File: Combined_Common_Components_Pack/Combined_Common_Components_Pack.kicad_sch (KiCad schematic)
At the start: 15 parts, among them J4 TP_hole_1.5mm, J5 TP_loop_2.54mm, J6 TP_pad_1mm, J8 Conn_01x03_Socket, K1 G5LE-1, Q12 2N7002K

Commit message: More circuits
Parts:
- added F5: 10mm Blade Fuse, Library:Fuseholder_Blade_Mini, symbol Device:Fuse
- F1: LCSC C22446878 -> C516070; Observations (none) -> 30V 200mA
- R83: Type SMD -> (none)
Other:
- note added: "Fuses"
- note added: "Optocoupler and LEDs"
- note added: "Signal, power switching, load protection"
- note removed: "Safety"
- moved on the sheet: BZ1, D26, D27, F2, H1, J4, J5, J6, J8, K1, Q12, R83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

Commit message: Added some connectors and basic parts
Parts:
- added F6: Polyfuse, Fuse:Fuse_1206_3216Metric_Pad1.42x1.75mm_HandSolder, symbol Device:Polyfuse
- added F7: Polyfuse, Fuse:Fuse_1210_3225Metric_Pad1.42x2.65mm_HandSolder, symbol Device:Polyfuse
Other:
- moved on the sheet: F2
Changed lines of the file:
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@@
+	)
+	(symbol
+		(lib_id "Device:Polyfuse")
+		(at 110.49 129.54 90)
+		(unit 1)
+		(exclude_from_sim no)
+		(in_bom yes)
+		(on_board yes)
+		(dnp no)
+		(property "Reference" "F6"
+			(at 106.426 132.334 90)
+			(effects
+				(font
+					(size 1.27 1.27)
+				)
+			)
+		)
+		(property "Value" "Polyfuse"
+			(at 112.268 132.334 90)
+			(effects
+				(font
+					(size 1.27 1.27)
+				)
+			)
+		)
+		(property "Footprint" "Fuse:Fuse_1206_3216Metric_Pad1.42x1.75mm_HandSolder"
+			(at 115.57 128.27 0)
+			(effects
+				(font
+					(size 1.27 1.27)
+				)
+				(justify left)
+				(hide yes)
+			)
+		)
+		(property "Datasheet" "~"
+			(at 110.49 129.54 0)
+			(effects
+				(font
+					(size 1.27 1.27)
+				)
+				(hide yes)
+			)
+		)
+		(property "Description" "Polymeric PTC Resettable Fuse 48V 200mA Surface Mount 1206"
+			(at 110.49 129.54 0)
+			(effects
+				(font
+					(size 1.27 1.27)
+				)
+				(hide yes)
+			)
+		)
+		(property "LCSC" "C22446878"
+			(at 110.49 129.54 0)
+			(effects
+				(font
+					(size 1.27 1.27)
+				)
+				(hide yes)
+			)
+		)
+		(property "Observations" "48V 200mA"
+			(at 110.49 127 90)
+			(effects
+				(font
+					(size 1.27 1.27)
+				)
+			)
+		)
+		(pin "1"
+		)
+		(pin "2"
+		)
+		(instances
+			(project "Combined_Common_Components_Pack"
+				(path "/59e42e8e-5444-465a-b7a8-ffbd342a8d49"
+					(reference "F6")
+					(unit 1)
+				)
+			)
+		)
 	)
 	(symbol
@@
 	)
 	(symbol
+		(lib_id "Device:Polyfuse")
+		(at 123.19 129.54 90)
+		(unit 1)
+		(exclude_from_sim no)
+		(in_bom yes)
+		(on_board yes)
+		(dnp no)
+		(property "Reference" "F7"
+			(at 119.126 132.334 90)
+			(effects
+				(font
+					(size 1.27 1.27)
+				)
+			)
+		)
+		(property "Value" "Polyfuse"
+			(at 124.968 132.334 90)
+			(effects
+				(font
+					(size 1.27 1.27)
+				)
+			)
+		)
+		(property "Footprint" "Fuse:Fuse_1210_3225Metric_Pad1.42x2.65mm_HandSolder"
+			(at 128.27 128.27 0)
+			(effects
+				(font
+					(size 1.27 1.27)
+				)
+				(justify left)
+				(hide yes)
+			)
+		)
+		(property "Datasheet" "https://www.lcsc.com/datasheet/C269167.pdf"
+			(at 123.19 129.54 0)
+			(effects
+				(font
+					(size 1.27 1.27)
+				)
+				(hide yes)
+			)
+		)
+		(property "Description" "Polymeric PTC Resettable Fuse 16V 1.5A Surface Mount 1210"
+			(at 123.19 129.54 0)
+			(effects
+				(font
+					(size 1.27 1.27)
+				)
+				(hide yes)
+			)
+		)
+		(property "LCSC" "C269167"
+			(at 123.19 129.54 0)
+			(effects
+				(font
+					(size 1.27 1.27)
+				)
+				(hide yes)
+			)
+		)
+		(property "Observations" "16V 1.5A"
+			(at 123.19 127 90)
+			(effects
+				(font
+					(size 1.27 1.27)
+				)
+			)
+		)
+		(pin "1"
+		)
+		(pin "2"
+		)
+		(instances
+			(project "Combined_Common_Components_Pack"
+				(path "/59e42e8e-5444-465a-b7a8-ffbd342a8d49"
+					(reference "F7")
+					(unit 1)
+				)
+			)
+		)
+	)
+	(symbol
 		(lib_id "Device:Fuse")
-		(at 96.52 138.43 270)
+		(at 96.52 142.24 270)
 		(mirror x)
 		(unit 1)
@@
 		(dnp no)
 		(property "Reference" "F2"
-			(at 96.52 135.89 90)
+			(at 96.52 139.7 90)
 			(effects
 				(font
@@
 		)
 		(property "Value" "20mm Fuse holder"
-			(at 96.52 140.97 90)
+			(at 96.52 144.78 90)
 			(effects
 				(font
@@
 		)
 		(property "Footprint" "Fuse:Fuseholder_Cylinder-5x20mm_Schurter_0031_8201_Horizontal_Open"
-			(at 96.52 140.208 90)
+			(at 96.52 144.018 90)
 			(effects
 				(font
@@
 		)
 		(property "Datasheet" "https://br.mouser.com/datasheet/2/87/Eaton_06202018__HTC_100M-1372276.pdf"
-			(at 96.52 138.43 0)
+			(at 96.52 142.24 0)
 			(effects
 				(font
@@
 		)
 		(property "Description" "Plugin Fuseholders ROHS"
-			(at 96.52 138.43 0)
+			(at 96.52 142.24 0)
 			(effects
 				(font
@@
 		)
 		(property "LCSC" "C3131"
-			(at 96.52 138.43 0)
+			(at 96.52 142.24 0)
 			(effects
 				(font
@@
 		)
 		(property "Manufacturer " "Xucheng Elec"
-			(at 96.52 138.43 0)
+			(at 96.52 142.24 0)
 			(effects
 				(font
@@
 		)
 		(property "Mfr. Part Number" "5x20 BLX-A  XC-7"
-			(at 96.52 138.43 0)
+			(at 96.52 142.24 0)
 			(effects
 				(font
@@
 		)
 		(property "Observations" "For 5x20mm glass fuse"
-			(at 96.52 138.43 0)
+			(at 96.52 142.24 0)
 			(effects
 				(font
@@
 			(project "Combined_Common_Components_Pack"
 				(path "/59e42e8e-5444-465a-b7a8-ffbd342a8d49"
-					(page "7")
+					(page "6")
 				)
 			)
@@
 			(project "Combined_Common_Components_Pack"
 				(path "/59e42e8e-5444-465a-b7a8-ffbd342a8d49"
-					(page "10")
+					(page "3")
 				)
 			)
@@
 			(project "Combined_Common_Components_Pack"
 				(path "/59e42e8e-5444-465a-b7a8-ffbd342a8d49"
-					(page "5")
+					(page "10")
 				)
 			)
@@
 			(project "Combined_Common_Components_Pack"
 				(path "/59e42e8e-5444-465a-b7a8-ffbd342a8d49"
-					(page "11")
+					(page "12")
 				)
 			)
@@
 			(project "Combined_Common_Components_Pack"
 				(path "/59e42e8e-5444-465a-b7a8-ffbd342a8d49"
-					(page "10")
+					(page "11")
 				)
 			)
@@
 			(project "Combined_Common_Components_Pack"
 				(path "/59e42e8e-5444-465a-b7a8-ffbd342a8d49"
-					(page "12")
+					(page "7")
 				)
 			)
@@
 			(project "Combined_Common_Components_Pack"
 				(path "/59e42e8e-5444-465a-b7a8-ffbd342a8d49"
-					(page "6")
-				)
-			)
+					(page "5")
+				)
+			)

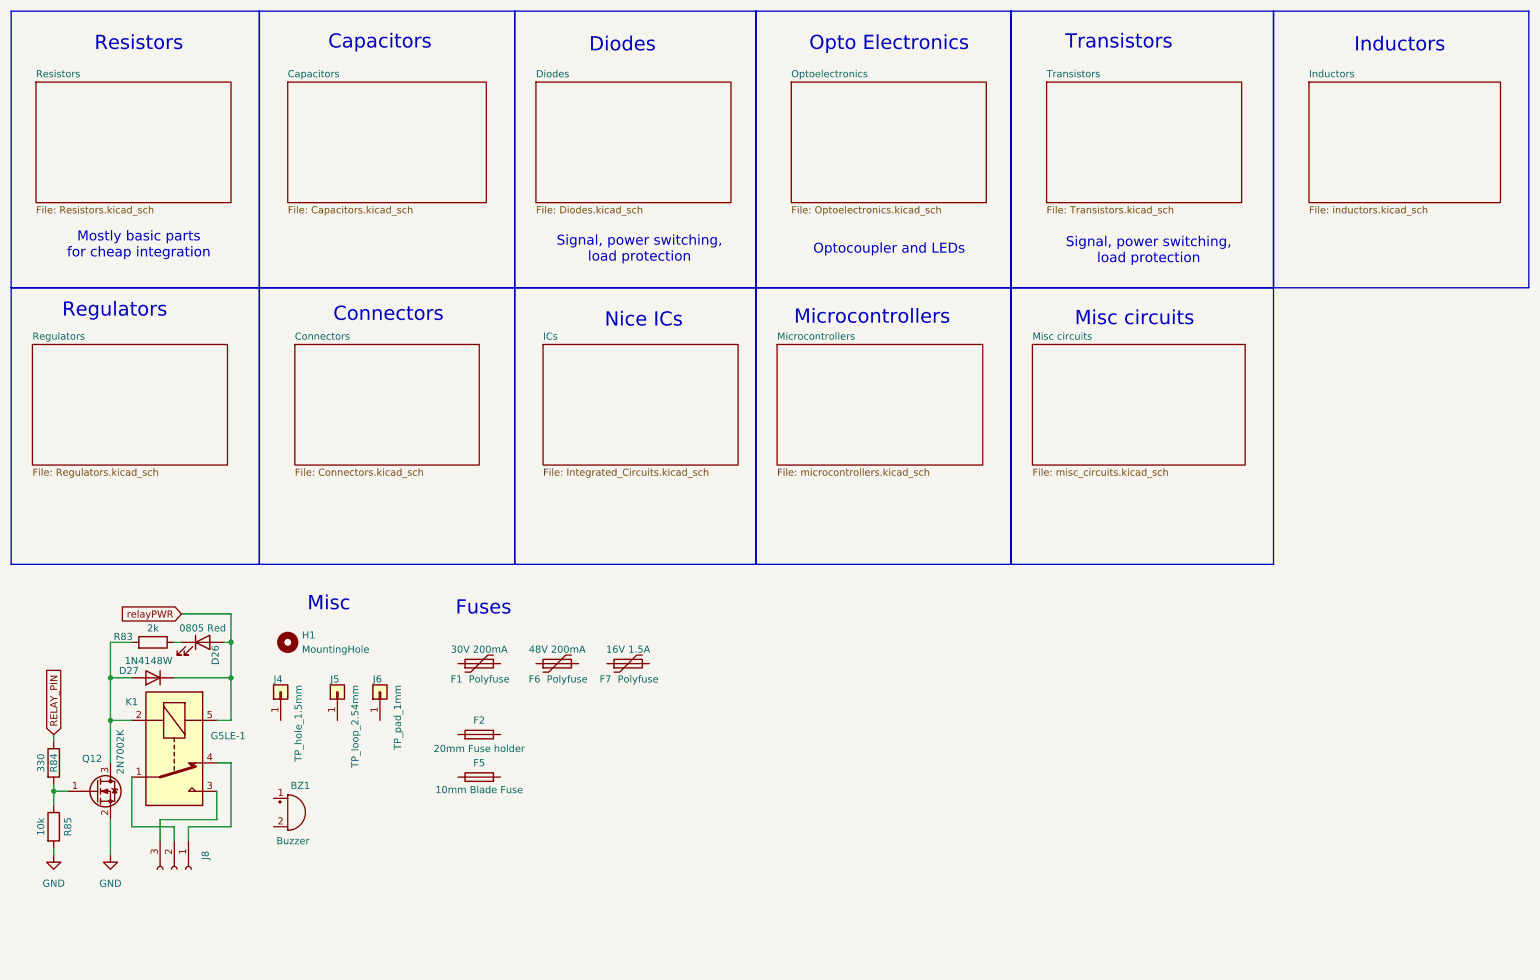
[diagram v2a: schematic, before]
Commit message: Minor updates
Basically components annotation, and more basic parts added
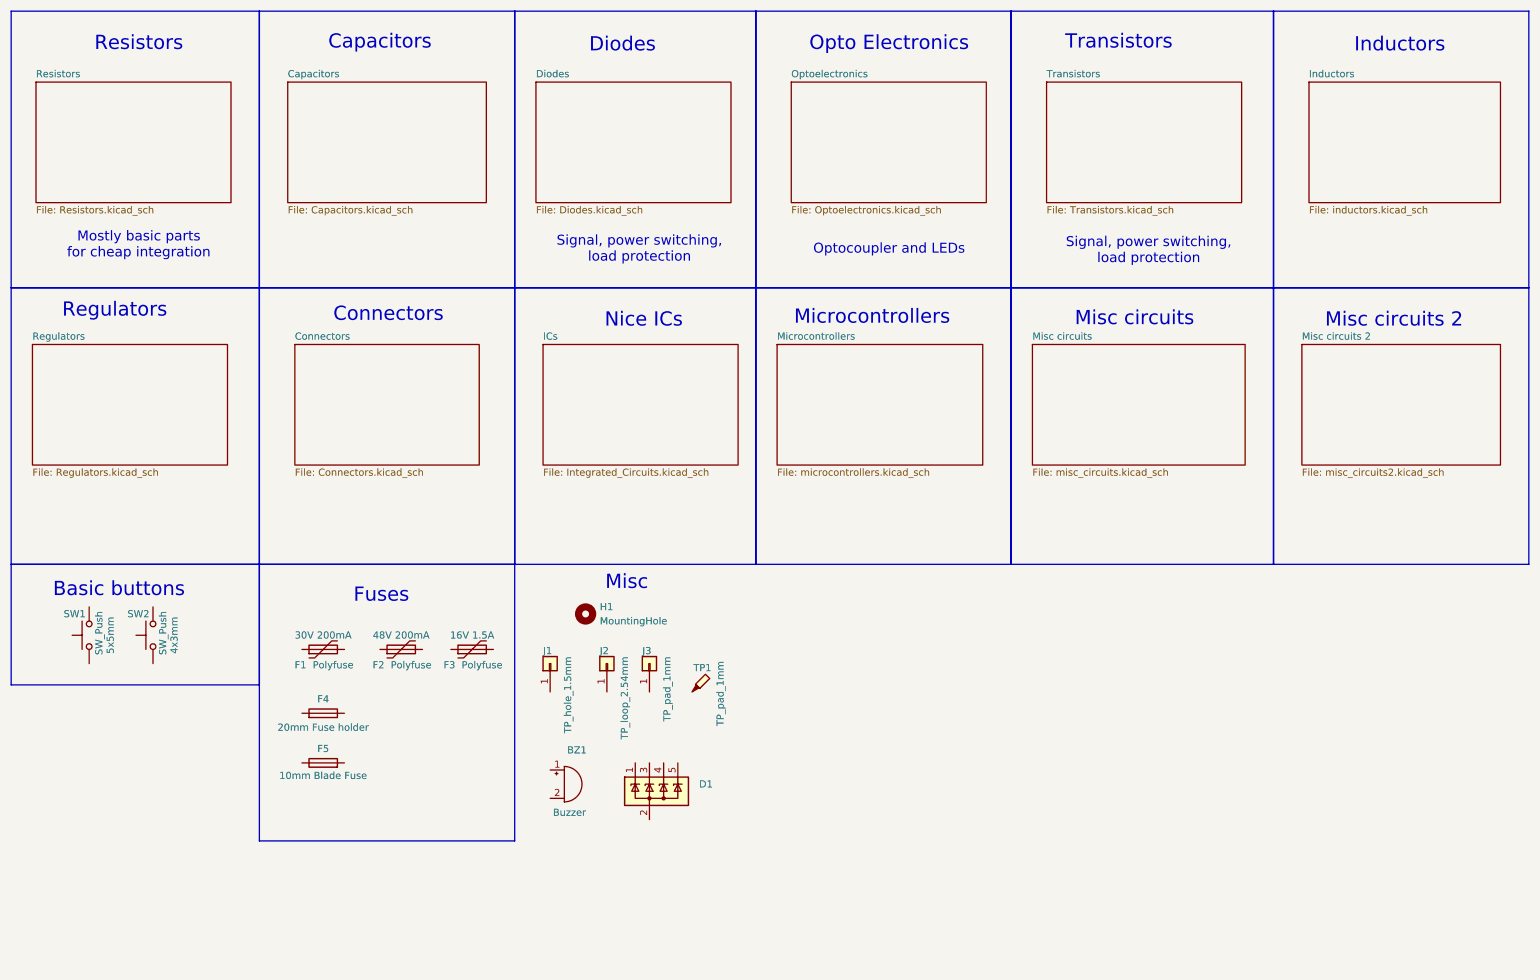
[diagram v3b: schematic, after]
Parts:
- removed D26: LED_RED, LED_SMD:LED_0805_2012Metric_Pad1.15x1.40mm_HandSolder, symbol Device:LED
- removed D27: 1N4148W, Diode_SMD:D_SOD-123, symbol Diode:1N4148W
- removed J8: Conn_01x03_Socket, Connector_JST:JST_NV_B03P-NV_1x03_P5.00mm_Vertical, symbol Connector:Conn_01x03_Socket
- removed K1: G5LE-1, Relay_THT:Relay_SPDT_Omron-G5LE-1, symbol Relay:G5LE-1
- removed Q12: 2N7002K, Package_TO_SOT_SMD:SOT-23, symbol Transistor_FET:2N7002K
- removed R83: 2k, Resistor_SMD:R_0402_1005Metric_Pad0.72x0.64mm_HandSolder, symbol 1_Library_GF:R_SMD_0805
- removed R84: 330, Resistor_SMD:R_0805_2012Metric, symbol Device:R
- removed R85: 10k, Resistor_SMD:R_0805_2012Metric, symbol Device:R
- added D1: SP0504BAHT, Package_TO_SOT_SMD:SOT-23-5, symbol Power_Protection:SP0504BAHT
- added SW1: SW_Push, Button_Switch_SMD:SW_SPST_SKQG_WithStem, symbol Switch:SW_Push
- added SW2: SW_Push, Button_Switch_SMD:SW_Push_SPST_NO_Alps_SKRK, symbol Switch:SW_Push
- added TP1: TP_pad_1mm, TestPoint:TestPoint_Pad_D1.0mm, symbol Connector:TestPoint_Probe
- renumbered F6 to F2, F7 to F3, F2 to F4, J4 to J1, J5 to J2, J6 to J3
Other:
- added sheet Misc circuits 2 (misc_circuits2.kicad_sch)
- note added: "Basic buttons"
- note added: "Misc circuits 2"
- moved on the sheet: BZ1, F1, F2, F3, F4, F5, H1, J1, J2, J3

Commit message: Minor updates
Started footprint library for easier cross-computer design management.
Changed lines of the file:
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@@
 (kicad_sch
-	(version 20231120)
+	(version 20250114)
 	(generator "eeschema")
-	(generator_version "8.0")
+	(generator_version "9.0")
 	(paper "A4")
 	(rectangle
@@
 		(at 106.68 25.4)
 		(size 34.925 21.59)
+		(exclude_from_sim no)
+		(in_bom yes)
+		(on_board yes)
+		(dnp no)
 		(fields_autoplaced yes)
 		(stroke
@@
 		(at 243.84 72.39)
 		(size 35.56 21.59)
+		(exclude_from_sim no)
+		(in_bom yes)
+		(on_board yes)
+		(dnp no)
 		(fields_autoplaced yes)
 		(stroke
@@
 		(at 198.12 25.4)
 		(size 34.925 21.59)
+		(exclude_from_sim no)
+		(in_bom yes)
+		(on_board yes)
+		(dnp no)
 		(fields_autoplaced yes)
 		(stroke
@@
 		(at 62.23 25.4)
 		(size 35.56 21.59)
+		(exclude_from_sim no)
+		(in_bom yes)
+		(on_board yes)
+		(dnp no)
 		(fields_autoplaced yes)
 		(stroke
@@
 		(at 107.95 72.39)
 		(size 34.925 21.59)
+		(exclude_from_sim no)
+		(in_bom yes)
+		(on_board yes)
+		(dnp no)
 		(fields_autoplaced yes)
 		(stroke
@@
 		(at 16.51 72.39)
 		(size 34.925 21.59)
+		(exclude_from_sim no)
+		(in_bom yes)
+		(on_board yes)
+		(dnp no)
 		(fields_autoplaced yes)
 		(stroke
@@
 		(at 195.58 72.39)
 		(size 38.1 21.59)
+		(exclude_from_sim no)
+		(in_bom yes)
+		(on_board yes)
+		(dnp no)
 		(fields_autoplaced yes)
 		(stroke
@@
 		(at 17.145 25.4)
 		(size 34.925 21.59)
+		(exclude_from_sim no)
+		(in_bom yes)
+		(on_board yes)
+		(dnp no)
 		(fields_autoplaced yes)
 		(stroke
@@
 		(at 63.5 72.39)
 		(size 33.02 21.59)
+		(exclude_from_sim no)
+		(in_bom yes)
+		(on_board yes)
+		(dnp no)
 		(fields_autoplaced yes)
 		(stroke
@@
 		(at 149.86 72.39)
 		(size 36.83 21.59)
+		(exclude_from_sim no)
+		(in_bom yes)
+		(on_board yes)
+		(dnp no)
 		(fields_autoplaced yes)
 		(stroke
@@
 		(at 245.11 25.4)
 		(size 34.29 21.59)
+		(exclude_from_sim no)
+		(in_bom yes)
+		(on_board yes)
+		(dnp no)
 		(fields_autoplaced yes)
 		(stroke
@@
 		(at 152.4 25.4)
 		(size 34.925 21.59)
+		(exclude_from_sim no)
+		(in_bom yes)
+		(on_board yes)
+		(dnp no)
 		(fields_autoplaced yes)
 		(stroke
@@
 		)
 	)
+	(embedded_fonts no)
 )

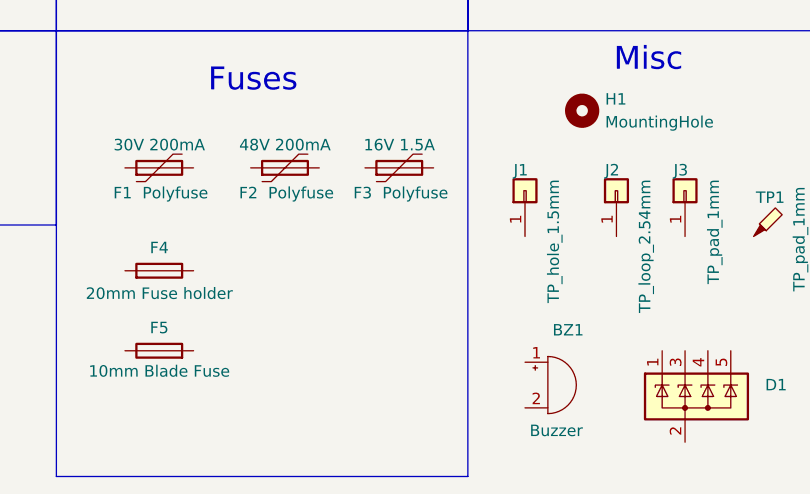
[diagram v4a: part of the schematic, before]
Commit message: Added XL4001 Load limiter devboard
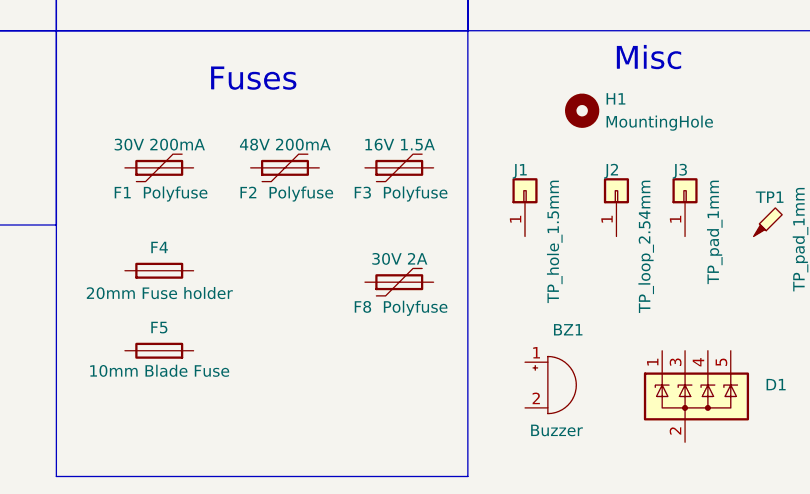
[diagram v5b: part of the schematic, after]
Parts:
- added F8: Polyfuse, Resistor_SMD:R_1812_4532Metric_Pad1.30x3.40mm_HandSolder, symbol Device:Polyfuse
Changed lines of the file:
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@@
+	)
+	(symbol
+		(lib_id "Device:Polyfuse")
+		(at 95.25 139.7 90)
+		(unit 1)
+		(exclude_from_sim no)
+		(in_bom yes)
+		(on_board yes)
+		(dnp no)
+		(property "Reference" "F8"
+			(at 91.186 142.494 90)
+			(effects
+				(font
+					(size 1.27 1.27)
+				)
+			)
+		)
+		(property "Value" "Polyfuse"
+			(at 97.028 142.494 90)
+			(effects
+				(font
+					(size 1.27 1.27)
+				)
+			)
+		)
+		(property "Footprint" "Resistor_SMD:R_1812_4532Metric_Pad1.30x3.40mm_HandSolder"
+			(at 100.33 138.43 0)
+			(effects
+				(font
+					(size 1.27 1.27)
+				)
+				(justify left)
+				(hide yes)
+			)
+		)
+		(property "Datasheet" "https://www.lcsc.com/datasheet/C269167.pdf"
+			(at 95.25 139.7 0)
+			(effects
+				(font
+					(size 1.27 1.27)
+				)
+				(hide yes)
+			)
+		)
+		(property "Description" "Polymeric PTC Resettable Fuse 30V 2A Surface Mount 1812"
+			(at 95.25 139.7 0)
+			(effects
+				(font
+					(size 1.27 1.27)
+				)
+				(hide yes)
+			)
+		)
+		(property "LCSC" "C2760293"
+			(at 95.25 139.7 0)
+			(effects
+				(font
+					(size 1.27 1.27)
+				)
+				(hide yes)
+			)
+		)
+		(property "Observations" "30V 2A"
+			(at 95.25 137.16 90)
+			(effects
+				(font
+					(size 1.27 1.27)
+				)
+			)
+		)
+		(pin "1"
+		)
+		(pin "2"
+		)
+		(instances
+			(project "Combined_Common_Components_Pack"
+				(path "/59e42e8e-5444-465a-b7a8-ffbd342a8d49"
+					(reference "F8")
+					(unit 1)
+				)
+			)
+		)
 	)
 	(symbol
